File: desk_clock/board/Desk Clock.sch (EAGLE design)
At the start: 14 parts, among them IC1 PIC16F628P, IC2 MAX7219CNG, U1 TMP75D, X1 22-23-2021

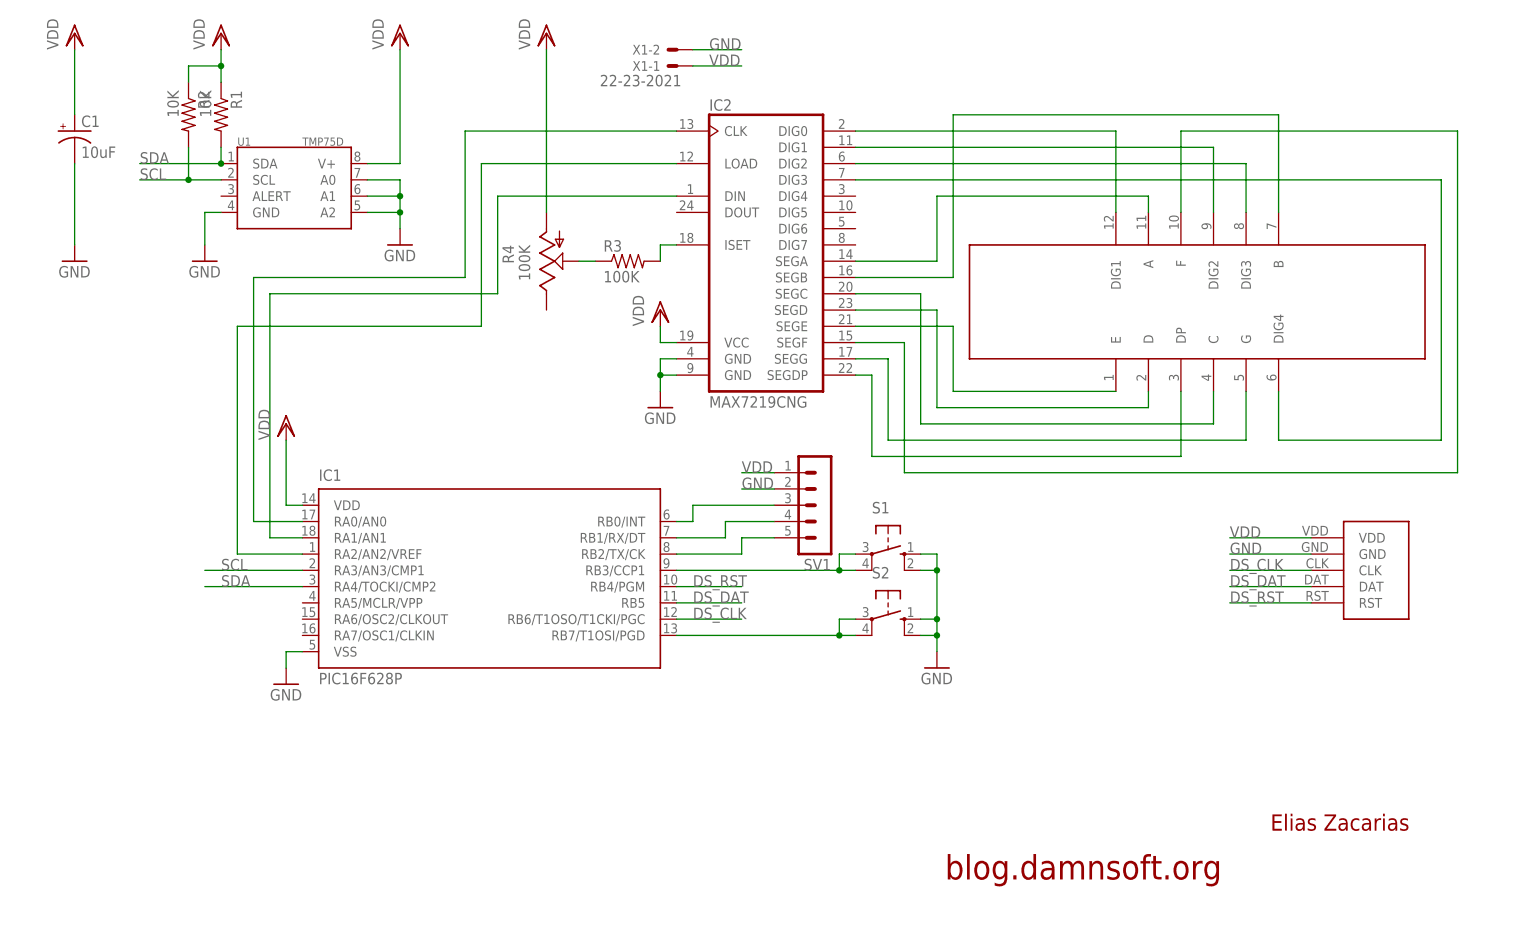
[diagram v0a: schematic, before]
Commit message: HW revision 1.1. Added a 0.1uF capacitor to improve electric stability and reduce drifting. Also removed version number from the pcb filenames (it's embedded in the schematic and pcb layout now). Firmware has been updated to deal with the random auto-halt of the DS1302 module in software, and the polling/refresh rate of the clock has been reduced by adding a delay in the loop. Some NOPs were removed from the DS1302 communication routines as they were not really needed due to the low frequency at which the PIC is running.
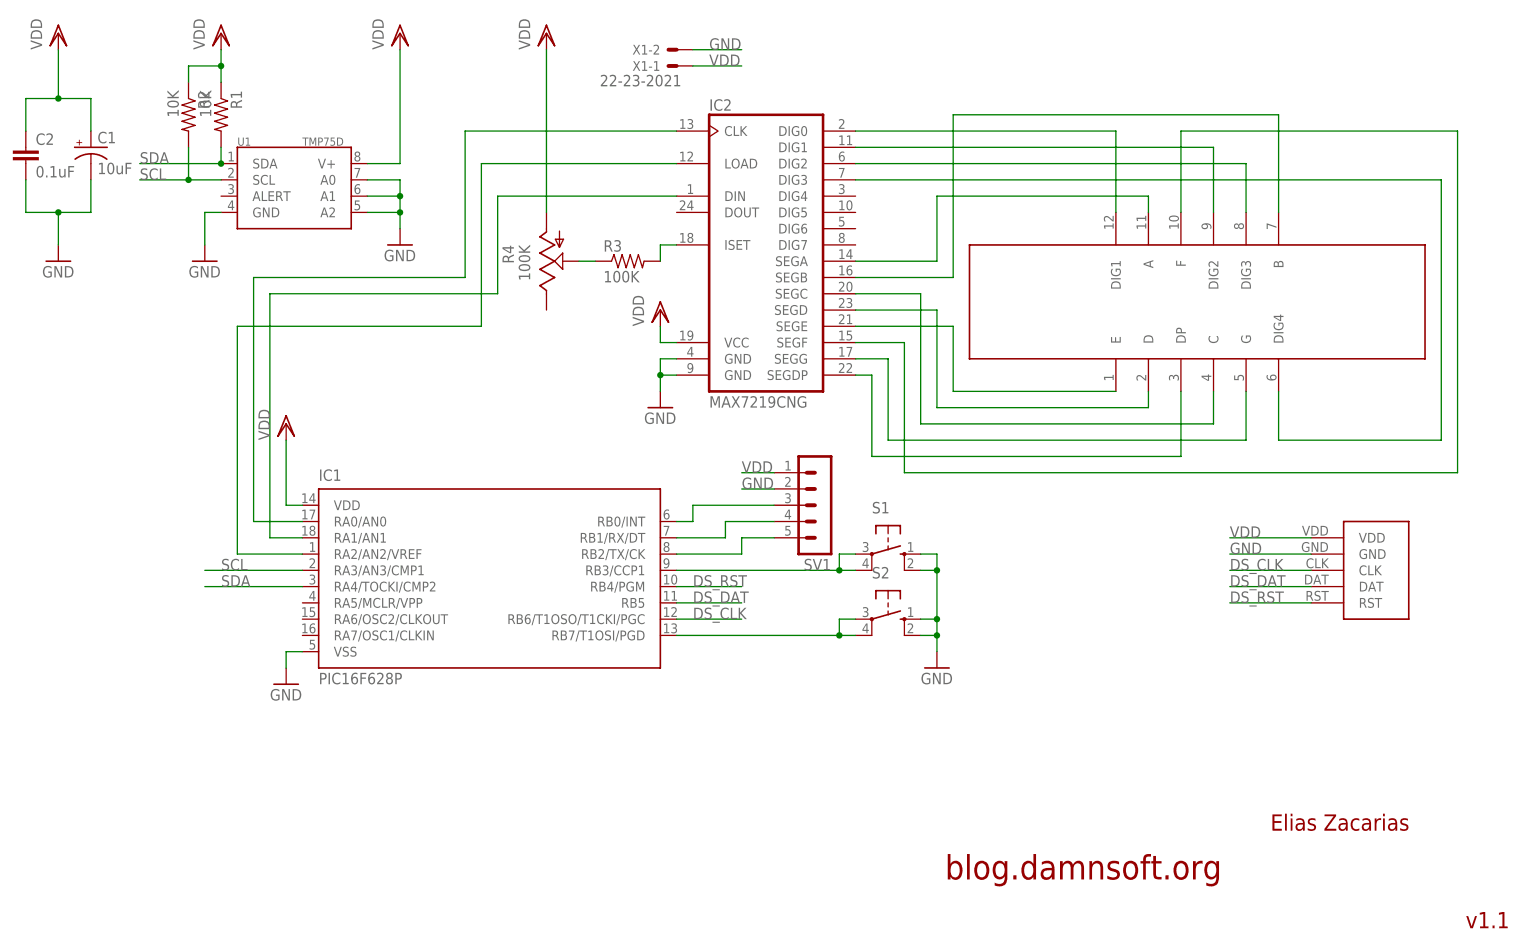
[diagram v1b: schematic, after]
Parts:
- added C2: 0.1uF, rcl:C-EU025-025X050
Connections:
- net GND: now also C2.2
- net VDD: now also C2.1
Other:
- note added: "v1.1"
- moved on the sheet: C1
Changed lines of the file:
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@@
 <part name="GND6" library="supply1" deviceset="GND" device=""/>
 <part name="FRAME1" library="frames" deviceset="A4L-LOC" device=""/>
+<part name="C2" library="rcl" deviceset="C-EU" device="025-025X050" value="0.1uF"/>
 </parts>
 <sheets>
@@
 <text x="168.91" y="-25.4" size="2.54" layer="94">Elias Zacarias</text>
 <text x="118.11" y="-33.02" size="3.81" layer="94">blog.damnsoft.org</text>
+<text x="199.39" y="-40.64" size="2.54" layer="94">v1.1</text>
 </plain>
 <instances>
@@
 <instance part="X1" gate="-2" x="76.2" y="96.52" rot="R180"/>
 <instance part="VDD5" gate="G$1" x="73.66" y="55.88"/>
-<instance part="C1" gate="G$1" x="-17.78" y="83.82"/>
-<instance part="VDD6" gate="G$1" x="-17.78" y="99.06"/>
-<instance part="GND6" gate="1" x="-17.78" y="63.5"/>
+<instance part="C1" gate="G$1" x="-15.24" y="81.28"/>
+<instance part="VDD6" gate="G$1" x="-20.32" y="99.06"/>
+<instance part="GND6" gate="1" x="-20.32" y="63.5"/>
 <instance part="FRAME1" gate="G$1" x="-48.26" y="-45.72" smashed="yes">
 <attribute name="DRAWING_NAME" x="168.91" y="-30.48" size="2.54" layer="94"/>
@@
 <attribute name="SHEET" x="182.245" y="-40.64" size="2.54" layer="94"/>
 </instance>
+<instance part="C2" gate="G$1" x="-25.4" y="81.28"/>
 </instances>
 <busses>
@@
 <segment>
 <pinref part="VDD6" gate="G$1" pin="VDD"/>
-<wire x1="-17.78" y1="96.52" x2="-17.78" y2="86.36" width="0.1524" layer="91"/>
+<wire x1="-20.32" y1="96.52" x2="-20.32" y2="88.9" width="0.1524" layer="91"/>
+<wire x1="-20.32" y1="88.9" x2="-15.24" y2="88.9" width="0.1524" layer="91"/>
+<wire x1="-15.24" y1="88.9" x2="-15.24" y2="83.82" width="0.1524" layer="91"/>
 <pinref part="C1" gate="G$1" pin="+"/>
+<pinref part="C2" gate="G$1" pin="1"/>
+<wire x1="-25.4" y1="83.82" x2="-25.4" y2="88.9" width="0.1524" layer="91"/>
+<wire x1="-25.4" y1="88.9" x2="-20.32" y2="88.9" width="0.1524" layer="91"/>
+<junction x="-20.32" y="88.9"/>
 </segment>
 </net>
@@
 <segment>
 <pinref part="GND6" gate="1" pin="GND"/>
-<wire x1="-17.78" y1="78.74" x2="-17.78" y2="66.04" width="0.1524" layer="91"/>
+<wire x1="-15.24" y1="76.2" x2="-15.24" y2="71.12" width="0.1524" layer="91"/>
+<wire x1="-15.24" y1="71.12" x2="-20.32" y2="71.12" width="0.1524" layer="91"/>
+<wire x1="-20.32" y1="71.12" x2="-20.32" y2="66.04" width="0.1524" layer="91"/>
 <pinref part="C1" gate="G$1" pin="-"/>
-</segment>
-</net>
+<pinref part="C2" gate="G$1" pin="2"/>
+<wire x1="-25.4" y1="76.2" x2="-25.4" y2="71.12" width="0.1524" layer="91"/>
+<wire x1="-25.4" y1="71.12" x2="-20.32" y2="71.12" width="0.1524" layer="91"/>
+<junction x="-20.32" y="71.12"/>
+</segment>
+</net>

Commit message: Hw revision 2.0 (compact board). Firmware updated to reflect that. Several small modifications made for better behavior.
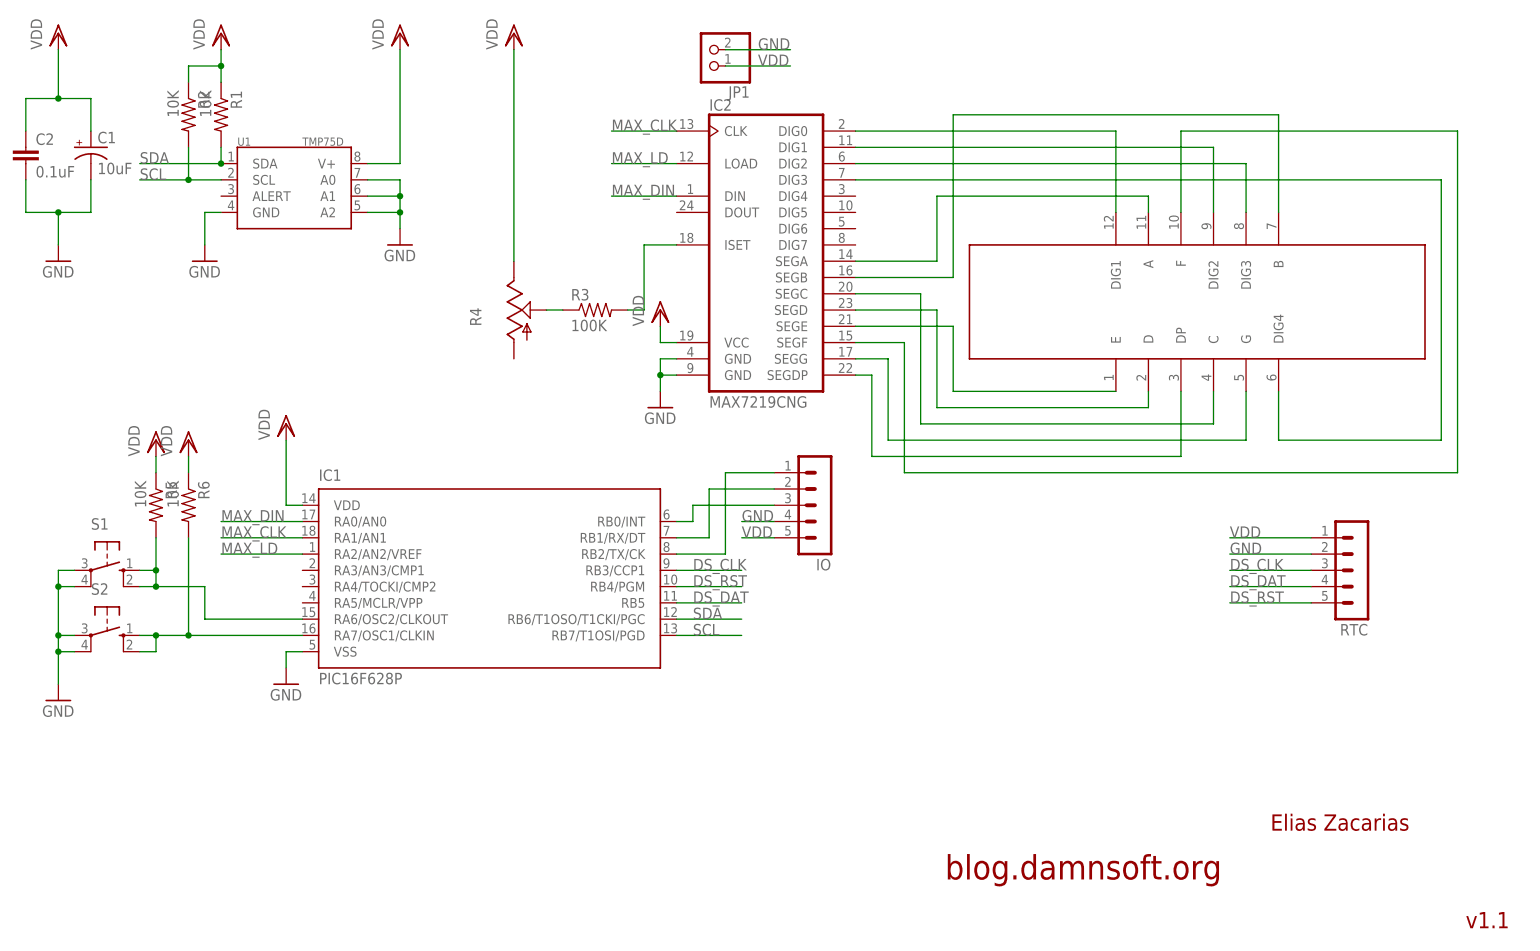
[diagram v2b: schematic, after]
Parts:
- removed U$2: DS1302_BOARD, DS1302_board:DS1302_BOARD
- removed X1: 22-23-2021, con-molex:22-23-2021
- added JP1: (no value), pinhead:PINHD-1X2
- added R5, R6: 10K, resistor:R-US_R0603
- added RTC: (no value), con-lstb:MA05-1
- R1, R2: device resistor:R-US_0207/10 -> resistor:R-US_R0603
- R3: device resistor:R-US_0207/10 -> resistor:R-US_0207/7
- R4: value 100K -> (none)
- renumbered SV1 to IO
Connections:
- net N$18 renamed INT
- net N$22 renamed MAX_LD
- removed net N$19: IC1.RA0/AN0, IC2.CLK
- removed net N$20: IC1.RB7/T1OSI/PGD, S2.P, S2.P1
- removed net N$21: IC1.RA1/AN1, IC2.DIN
- removed net N$9: IC1.RB3/CCP1, S1.P, S1.P1
- new net $N18: IC1.RA6/OSC2/CLKOUT, R5.2, S1.S, S1.S1
- new net $N9: IC1.RA7/OSC1/CLKIN, R6.2, S2.S, S2.S1
- new net MAX_CLK: IC1.RA1/AN1, IC2.CLK
- new net MAX_DIN: IC1.RA0/AN0, IC2.DIN
- net DS_CLK: now also IC1.RB3/CCP1, RTC.3; no longer IC1.RB6/T1OSO/T1CKI/PGC, U$2.CLK
- net DS_DAT: now also RTC.4; no longer U$2.DAT
- net DS_RST: now also RTC.5; no longer U$2.RST
- net GND: now also IO.4, JP1.2, RTC.2, S1.P, S1.P1, S2.P, S2.P1; no longer IO.2, S1.S, S1.S1, S2.S, S2.S1, U$2.GND, X1-2.S
- net N$16: now also IO.1; no longer IO.5
- net N$17: now also IO.2; no longer IO.4
- net SCL: now also IC1.RB7/T1OSI/PGD; no longer IC1.RA3/AN3/CMP1
- net SDA: now also IC1.RB6/T1OSO/T1CKI/PGC; no longer IC1.RA4/TOCKI/CMP2
- net VDD: now also IO.5, JP1.1, R4.E, R5.1, R6.1, RTC.1; no longer IO.1, R4.A, U$2.VDD, X1-1.S
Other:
- moved on the sheet: R3, R4, S1, S2
